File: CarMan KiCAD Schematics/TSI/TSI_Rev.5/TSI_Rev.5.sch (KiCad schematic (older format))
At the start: 23 parts, among them J25 Current_Sensor, J26 Conn_02x12_Counter_Clockwise

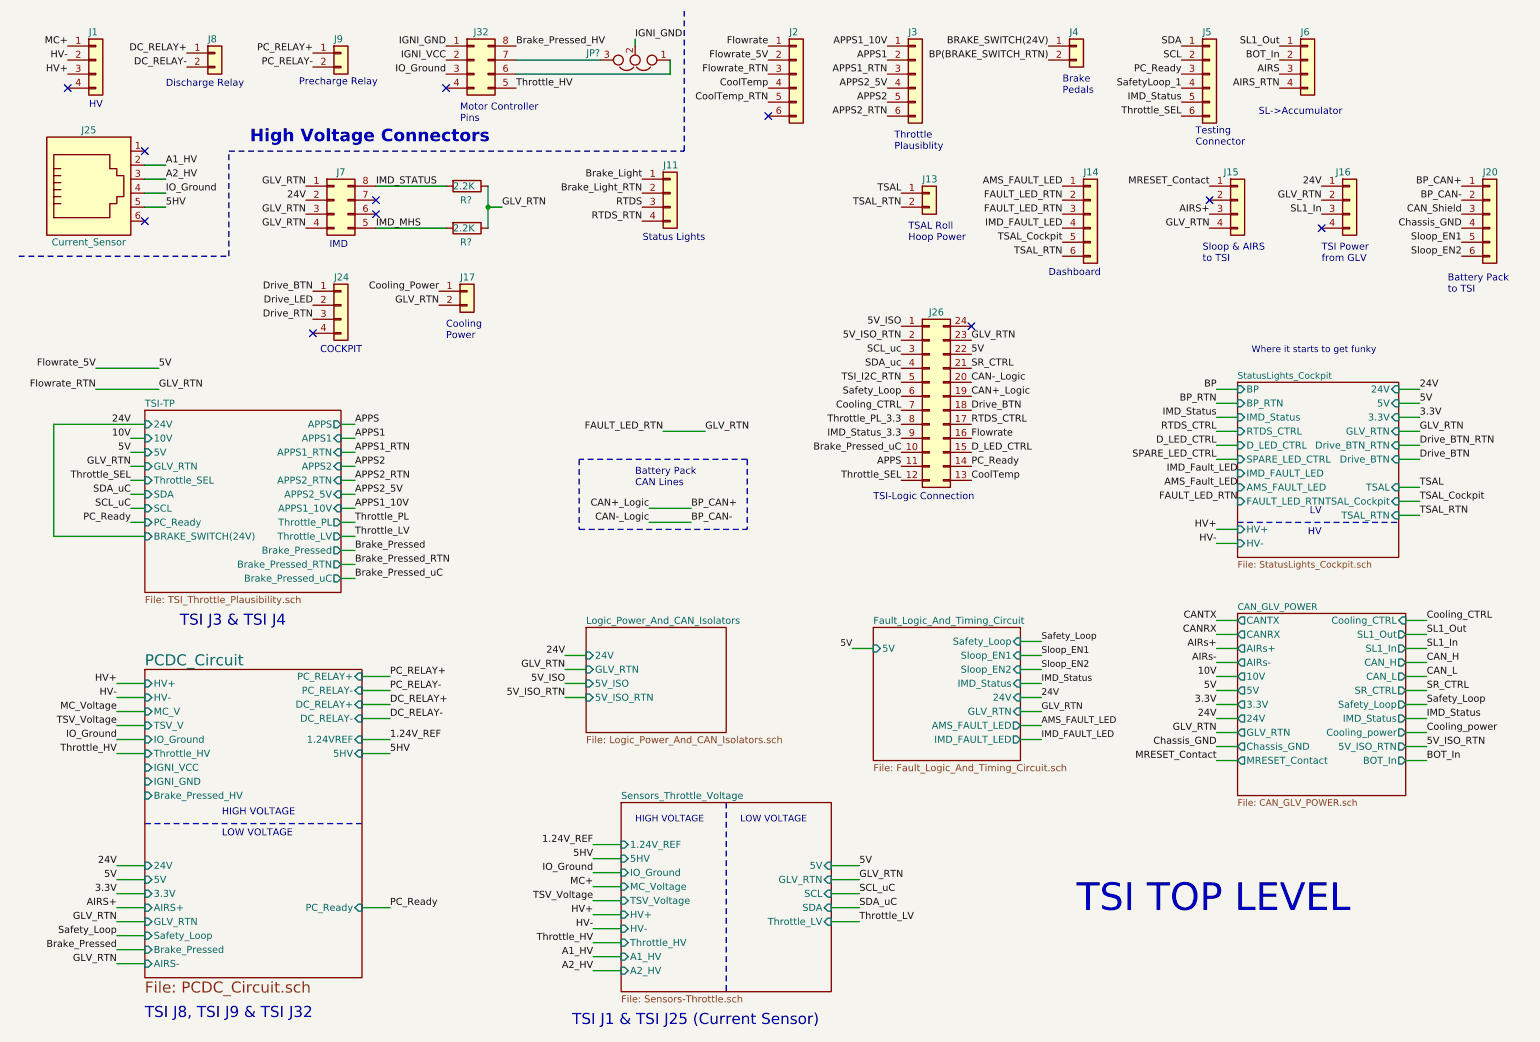
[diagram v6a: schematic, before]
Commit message: TSI Re-labeling
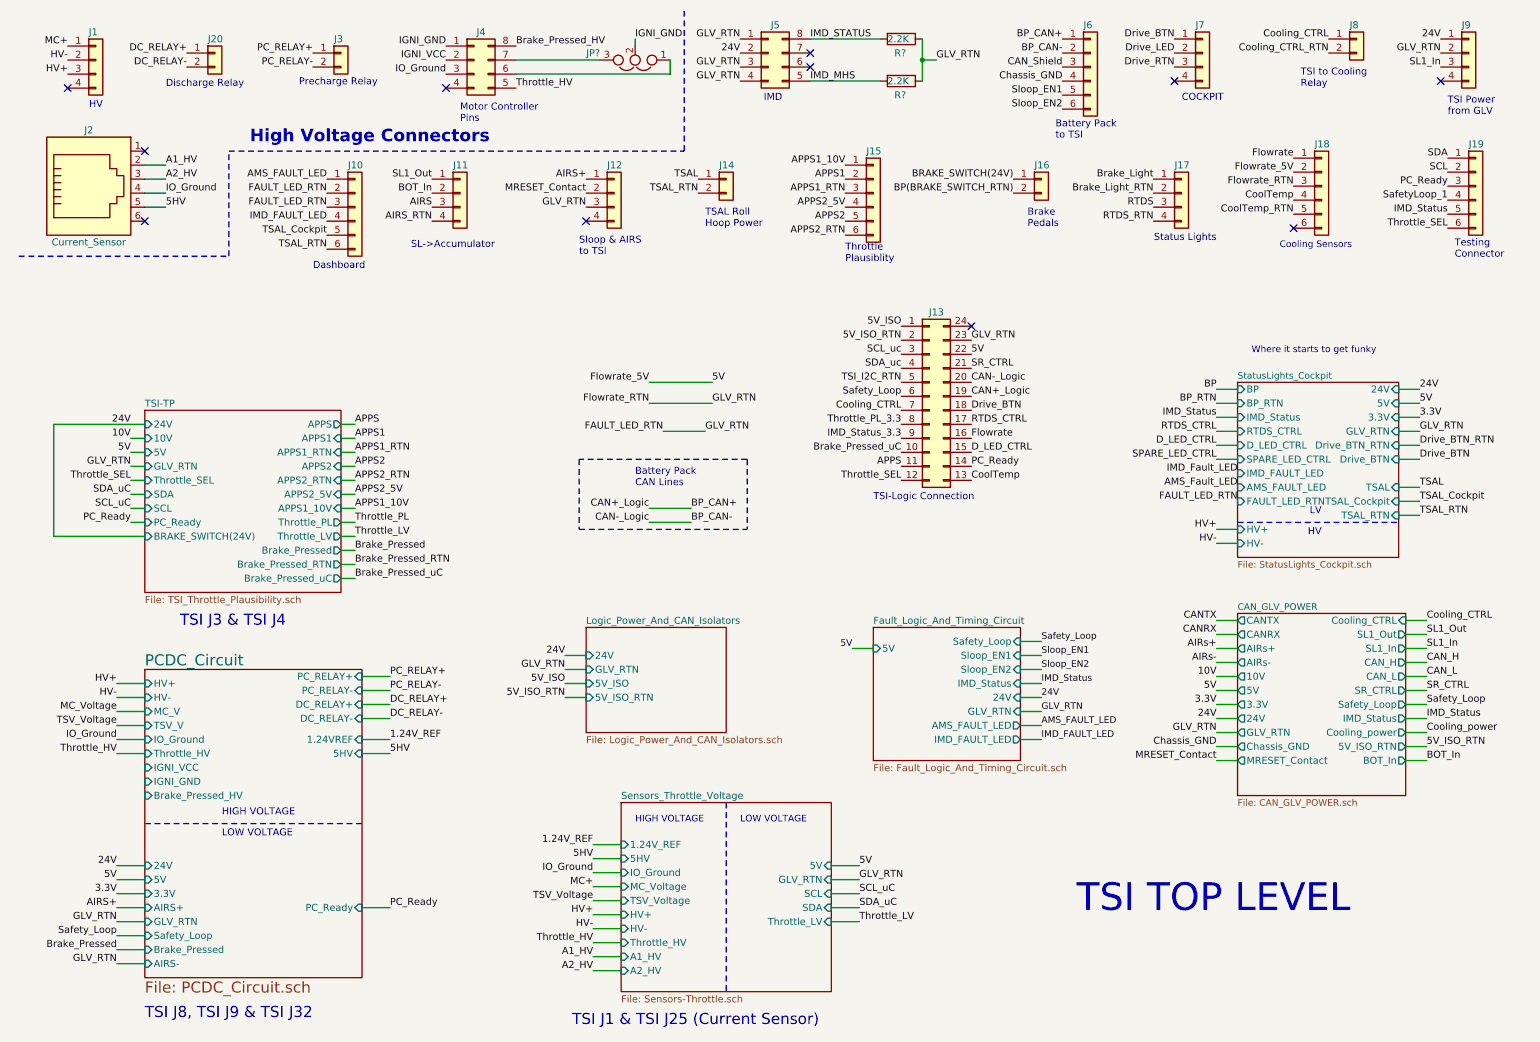
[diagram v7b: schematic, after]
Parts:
- J?: value J20 -> J6
- J?: value J17 -> J8
- J?: value J14 -> J10
- J?: value J13 -> J14
- J?: value J16 -> J9
- J?: value J2 -> J18
- J?: value J3 -> J15
- J?: value J4 -> J16
- J?: value J5 -> J19
- J?: value J6 -> J11
- J?: value J8 -> J20
- J?: value J9 -> J3
- J?: value J11 -> J17
- J?: value J15 -> J12
- J?: value J24 -> J7
- J?: value J7 -> J5
- J?: value J32 -> J4
- renumbered J26 to J13, J25 to J2
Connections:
- net Cooling_Power is gone; now on net Cooling_CTRL: J?.1 (Pin_1)
- net AIRS+: now also J?.1 (Pin_1); no longer J?.3 (Pin_3)
- net FAULT_LED_RTN: now also J?.3 (Pin_3); no longer J?.2 (Pin_2), J?.4 (Pin_4)
- net MRESET_Contact: now also J?.2 (Pin_2); no longer J?.1 (Pin_1)
- new net Cooling_CTRL_RTN: J?.2 (Pin_2)
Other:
- note added: "Cooling Sensors\n"
- note added: "TSI to Cooling\nRelay\n"
- note removed: "Cooling\nPower"
- moved on the sheet: R?

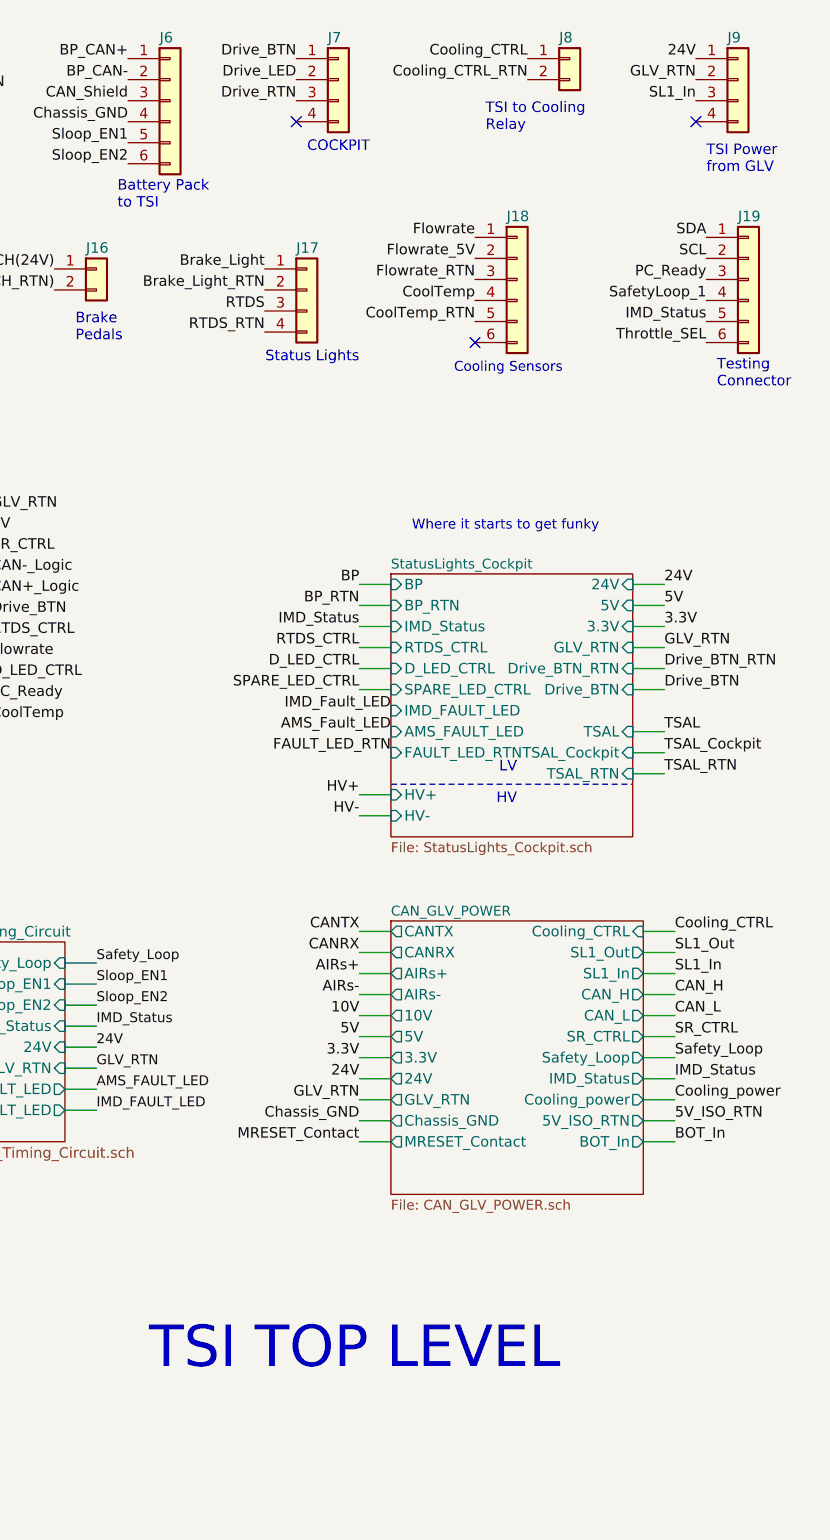
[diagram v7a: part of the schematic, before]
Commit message: TSI with Cooling + Scada Relay, new Cooling Connector
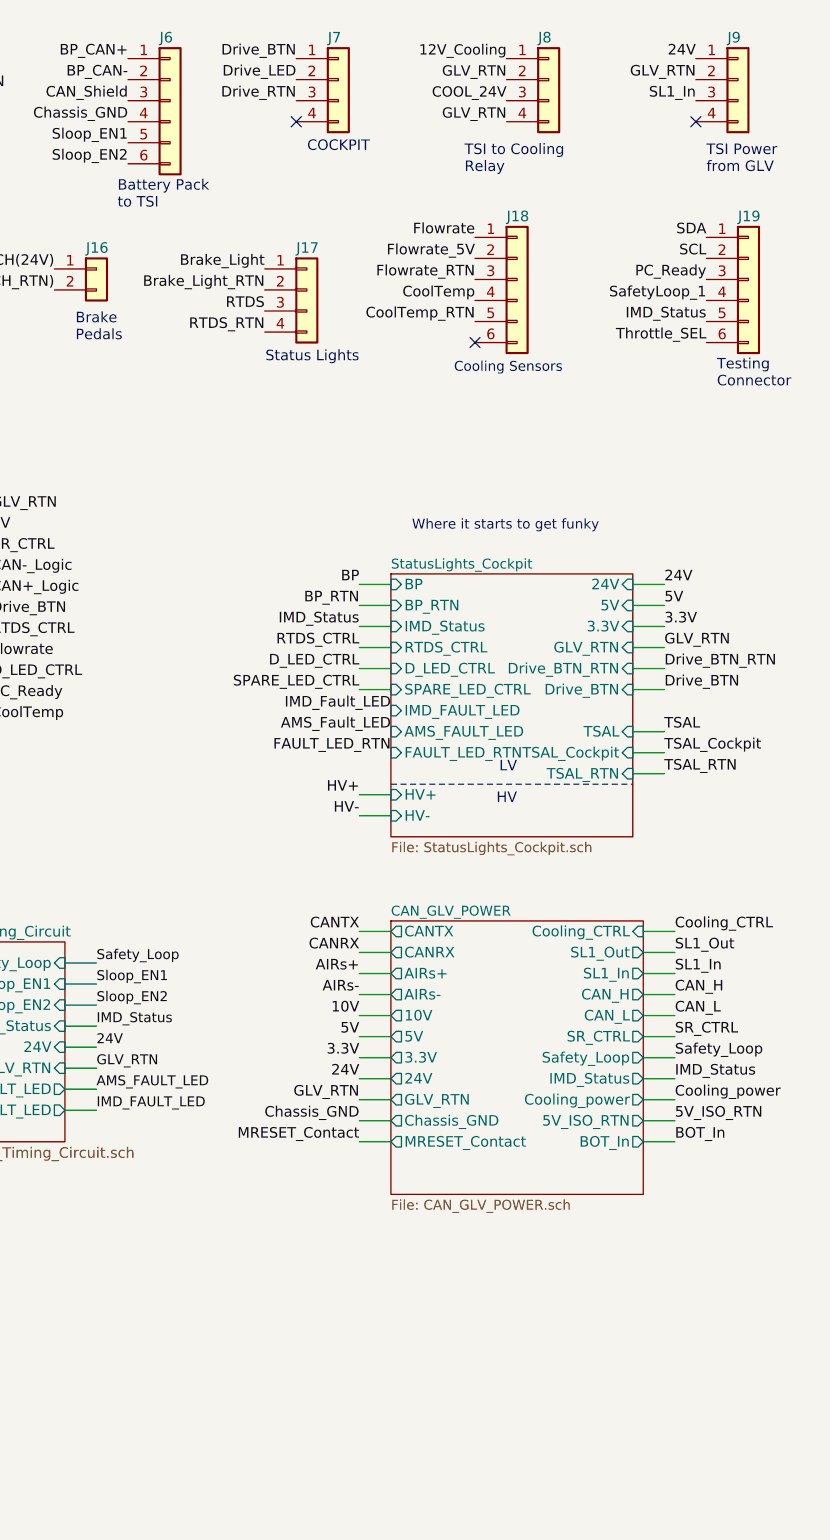
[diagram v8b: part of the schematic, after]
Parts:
- removed J?: J8, symbol Connector_Generic:Conn_01x02
- added J?: J8, symbol Connector_Generic:Conn_01x04
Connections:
- net FAULT_LED_RTN: now also J?.2 (Pin_2), J?.4 (Pin_4)
- new net 12V_Cooling: J?.1 (Pin_1)
- new net COOL_24V: J?.3 (Pin_3)
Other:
- note removed: "TSI TOP LEVEL\n"
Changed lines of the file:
@@
 encoding utf-8
 Sheet 1 8
-Title ""
+Title "TSI"
 Date ""
 Rev ""
 Comp ""
-Comment1 ""
+Comment1 "Authors: Nate Beal, John Burk, Ethan Miller, Troy Coleman, Zachary Martin"
 Comment2 ""
 Comment3 ""
@@
 Wire Notes Line
 	5500 6100 5500 7450
-Text Notes 9600 1000 0    50   ~ 0
+Text Notes 9500 1200 0    50   ~ 0
 TSI to Cooling\nRelay\n
-Text Label 9800 650  2    50   ~ 0
-Cooling_CTRL
-Text Label 9800 750  2    50   ~ 0
-Cooling_CTRL_RTN
-$Comp
-L Connector_Generic:Conn_01x02 J?
-U 1 1 5F9C2850
-P 10000 650
-F 0 "J?" H 10080 642 50  0001 L CNN
-F 1 "J8" H 9950 750 50  0000 L CNN
-F 2 "" H 10000 650 50  0001 C CNN
-F 3 "~" H 10000 650 50  0001 C CNN
-	1    10000 650
-	1    0    0    -1
-$EndComp
 $Comp
 L Connector_Generic:Conn_02x12_Counter_Clockwise J13
@@
 Text Label 10600 850  2    50   ~ 0
 SL1_In
-Text Notes 8000 6900 0    197  ~ 0
-TSI TOP LEVEL\n
 Wire Wire Line
 	3100 5400 2900 5400
@@
 Text Label 9550 1500 2    50   ~ 0
 Flowrate
+$Comp
+L Connector_Generic:Conn_01x04 J?
+U 1 1 5FBF6C81
+P 9900 750
+F 0 "J?" H 9980 742 50  0001 L CNN
+F 1 "J8" H 9850 950 50  0000 L CNN
+F 2 "" H 9900 750 50  0001 C CNN
+F 3 "~" H 9900 750 50  0001 C CNN
+	1    9900 750
+	1    0    0    -1
+$EndComp
+Text Label 9700 650  2    49   ~ 0
+12V_Cooling
+Text Label 9700 750  2    49   ~ 0
+GLV_RTN
+Text Label 9700 850  2    49   ~ 0
+COOL_24V
+Text Label 9700 950  2    49   ~ 0
+GLV_RTN
 $EndSCHEMATC
